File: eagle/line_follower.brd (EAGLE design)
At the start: 100 x 80 mm, 41 parts, among them IC1 A4950, IC2 A4950, IC3 MC78M05 (??), J1 2S - 4S LiPo, J2 22-27-2031-03, J3 22-27-2061-06, J4 22-27-2061-06, Q1 ALS-PT19-315C/L177/TR8, Q2 ALS-PT19-315C/L177/TR8, Q3 ALS-PT19-315C/L177/TR8, Q4 ALS-PT19-315C/L177/TR8, Q5 ALS-PT19-315C/L177/TR8, SW1 12MM_BUTTON, X1 ESP32DEVKITV1, X2 MPU6050_BREAKOUT

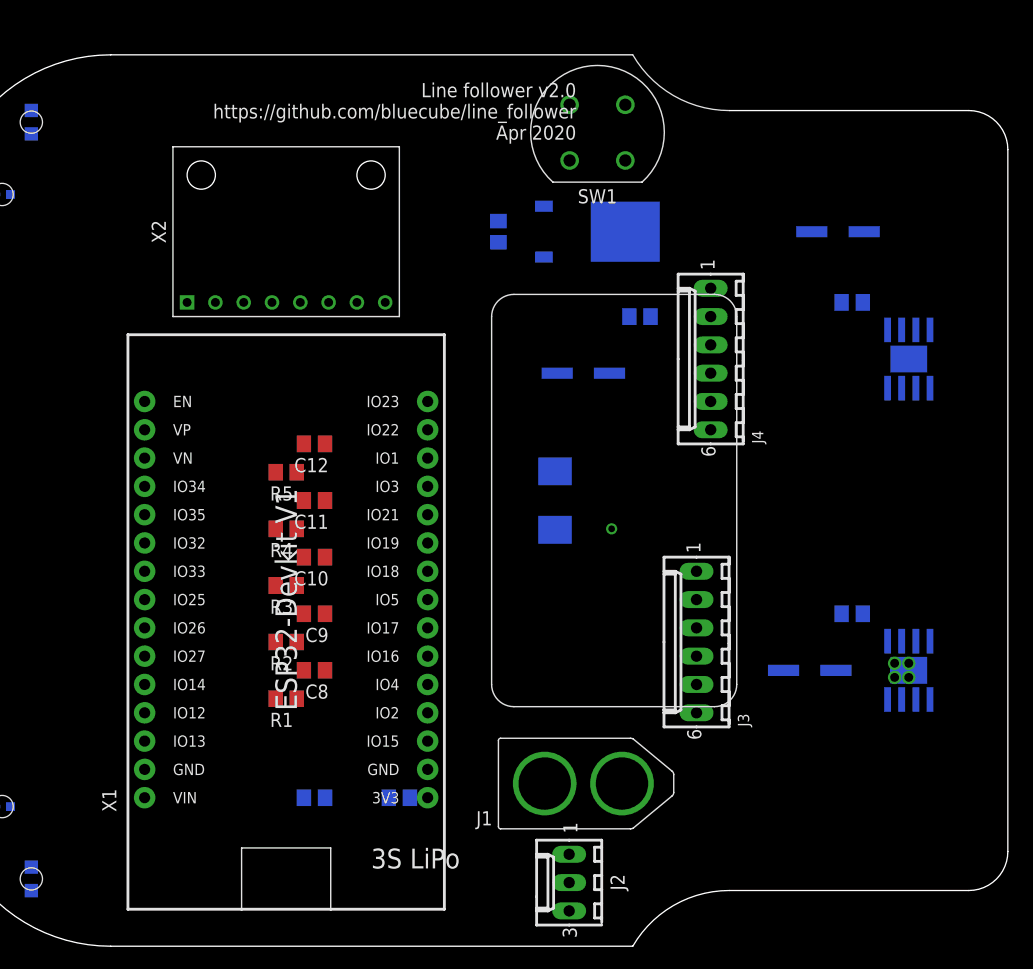
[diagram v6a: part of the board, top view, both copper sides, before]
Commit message: Decided to not use the encoder board on the motors, schematic tweaks and start of layout
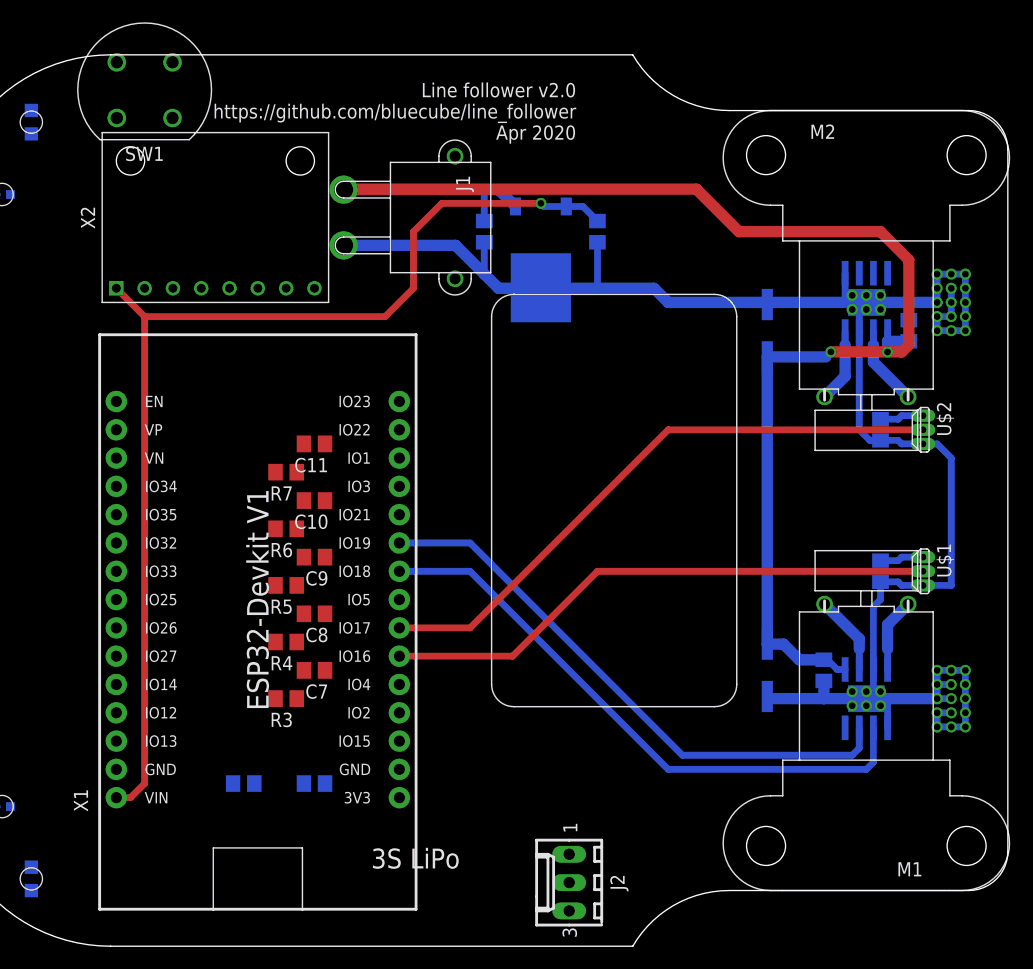
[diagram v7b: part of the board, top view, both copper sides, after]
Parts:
- removed D1: (no value), diode:MELF-MLL41
- removed J3, J4: 22-27-2061-06, con-molex:6410-06
- removed R10: 15k, rcl:R0805
- removed R9: 82k, rcl:R0805
- added C13: 100nF, rcl:C0805
- added M1, M2: N20-ENC, untitled:N20-ENC
- added R6, R7: 5k6, rcl:R0805
- added U$1, U$2: SI7202, untitled:TO92S
- C12: value 100n -> 100nF
- C2: value 100uF 25V -> 100nF; device rcl:UD-6,3X5,8_NICHICON -> rcl:C0805
- C6: value 100nF -> 22uF
- C7: value 100nF -> 100n
- IC3: value MC78M05 (??) -> NCV4274CDT50RKG
- J1: value 2S - 4S LiPo -> XT60PW-M; device RoboJackets-Connectors:XT-60_BARE -> untitled:XT60PW-M
- R1: value 5k6 -> 15k
- R2: value 5k6 -> 82k
- moved J1 51.6 mm to (45.7, 64.8)
- moved C12 50.8 mm to (88.9, 45.7), flipped to the bottom, turned to 270 degrees
- moved C5 47.6 mm to (53.3, 63.5), turned to 270 degrees
- moved C7 42.7 mm to (38.1, 24.1), flipped to the top, turned to 180 degrees
- moved SW1 40.8 mm to (22.9, 76.2)
- moved C1 31.4 mm to (78.7, 24.1), turned to 90 degrees
- moved C4 24.2 mm to (91.4, 54.6), turned to 90 degrees
- moved C6 23.7 mm to (63.5, 63.5), turned to 270 degrees
- moved R2 13.0 mm to (38.1, 14.0), flipped to the bottom, turned to 0 degrees
- moved C3 10.9 mm to (78.7, 54.6), turned to 270 degrees
- moved R3 10.2 mm to (35.6, 21.6)
- moved R4 10.2 mm to (35.6, 26.7)
- moved R5 10.2 mm to (35.6, 31.8)
- moved R1 8.52 mm to (31.8, 14.0), flipped to the bottom, turned to 0 degrees
- moved X2 6.48 mm to (29.2, 64.8)
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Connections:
- removed net ENCODER0A: J3.3
- removed net ENCODER0B: J3.4
- removed net ENCODER1A: J4.4, X1.28
- removed net ENCODER1B: J4.3, X1.6
- removed net N$6: C7.1, D1.A, IC3.2
- removed net N$7: C4.1, IC3.1
- removed net VCC: C2.+, C3.+, C5.1, C6.1, IC1.5, IC2.5, J1.+, R9.1
- new net ENCODER0: U$2.P$2, X1.7
- new net ENCODER1: U$1.P$2, X1.6
- new net VBAT: C1.+, C2.1, C3.+, C4.1, C5.1, IC1.5, IC2.5, IC3.1, J1.POS, R2.1
- net +3V3: now also C12.1, C13.1, U$1.P$1, U$2.P$1; no longer J3.2, J4.2
- net +5V: now also C6.1, IC3.2; no longer C1.+, D1.C
- net BAT_SENSE: now also R1.1, R2.2; no longer R10.1, R9.2
- net GND: now also C12.2, C13.2, C2.2, C7.1, J1.NEG, R1.2, R6.1, R7.1, U$1.P$3, U$2.P$3; no longer C12.1, C2.-, C7.2, J1.-, J3.5, J4.5, R1.1, R10.2, R2.1
- net LINE_SENSOR0: now also C7.2, R3.2; no longer C8.2, R1.2
- net LINE_SENSOR1: now also C8.2, R4.2; no longer C9.2, R2.2
- net LINE_SENSOR2: now also C9.2, R5.2; no longer C10.2, R3.2
- net LINE_SENSOR3: now also C10.2, R6.2; no longer C11.2, R4.2
- net LINE_SENSOR4: now also C11.2, R7.2; no longer C12.2, R5.2
- net MOTOR1A: now also X1.15
- net N$1: now also M1.P$2; no longer J3.1
- net N$2: now also M2.P$2; no longer J4.1
- net N$3: now also M2.P$1; no longer J4.6
- net N$4: now also M1.P$1; no longer J3.6
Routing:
- net GND: track 4.71 -> 181.5 mm, vias 4 -> 42
- net VBAT: track 0.00 -> 130.5 mm, vias 0 -> 2
- net +5V: track 0.00 -> 97.1 mm, vias 0 -> 1
- net ENCODER0: track 0.00 -> 54.4 mm
- net MOTOR0B: track 0.00 -> 53.3 mm
- net MOTOR0A: track 0.00 -> 51.3 mm
- net ENCODER1: track 0.00 -> 50.1 mm
- net +3V3: track 0.00 -> 7.89 mm
- net N$1: track 0.00 -> 7.15 mm
- net N$2: track 0.00 -> 7.15 mm
- net N$4: track 0.00 -> 6.63 mm
- net N$3: track 0.00 -> 6.63 mm

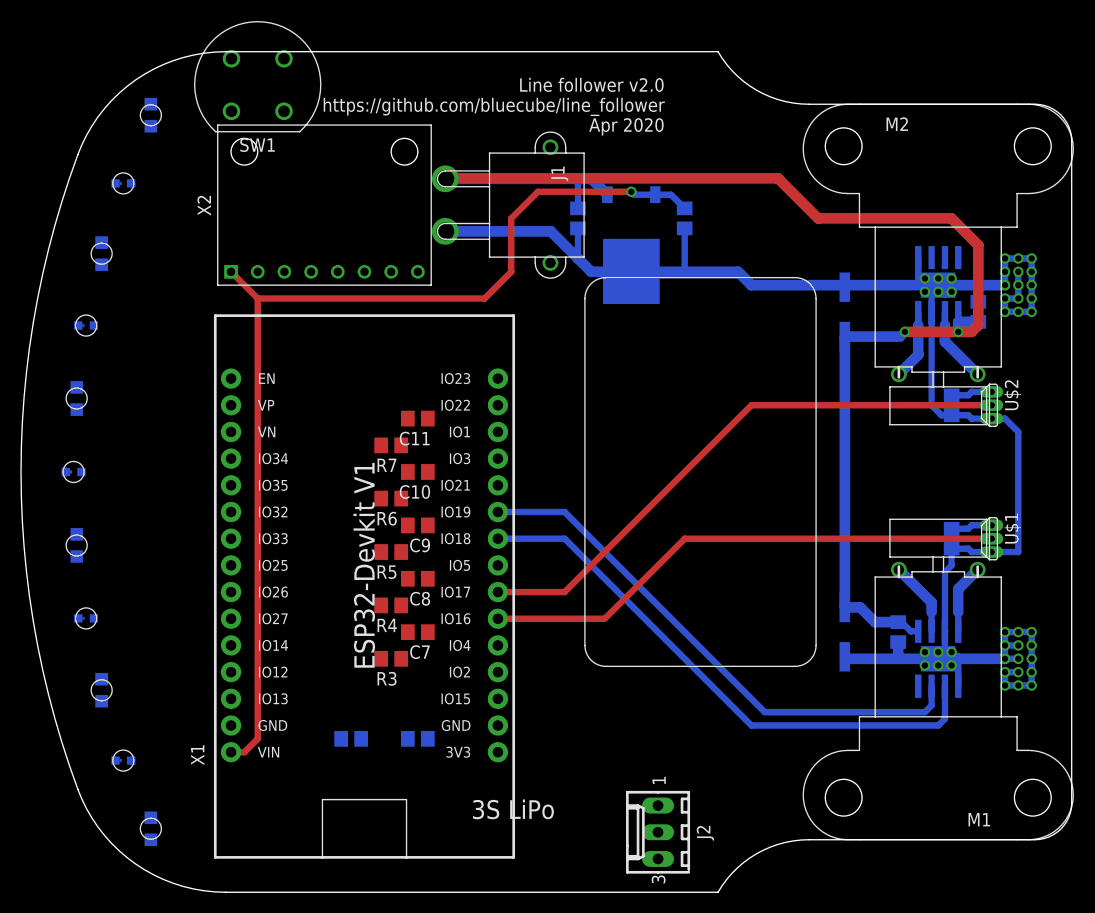
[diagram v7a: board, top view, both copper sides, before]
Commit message: Motor encoder boards are back, more layout work
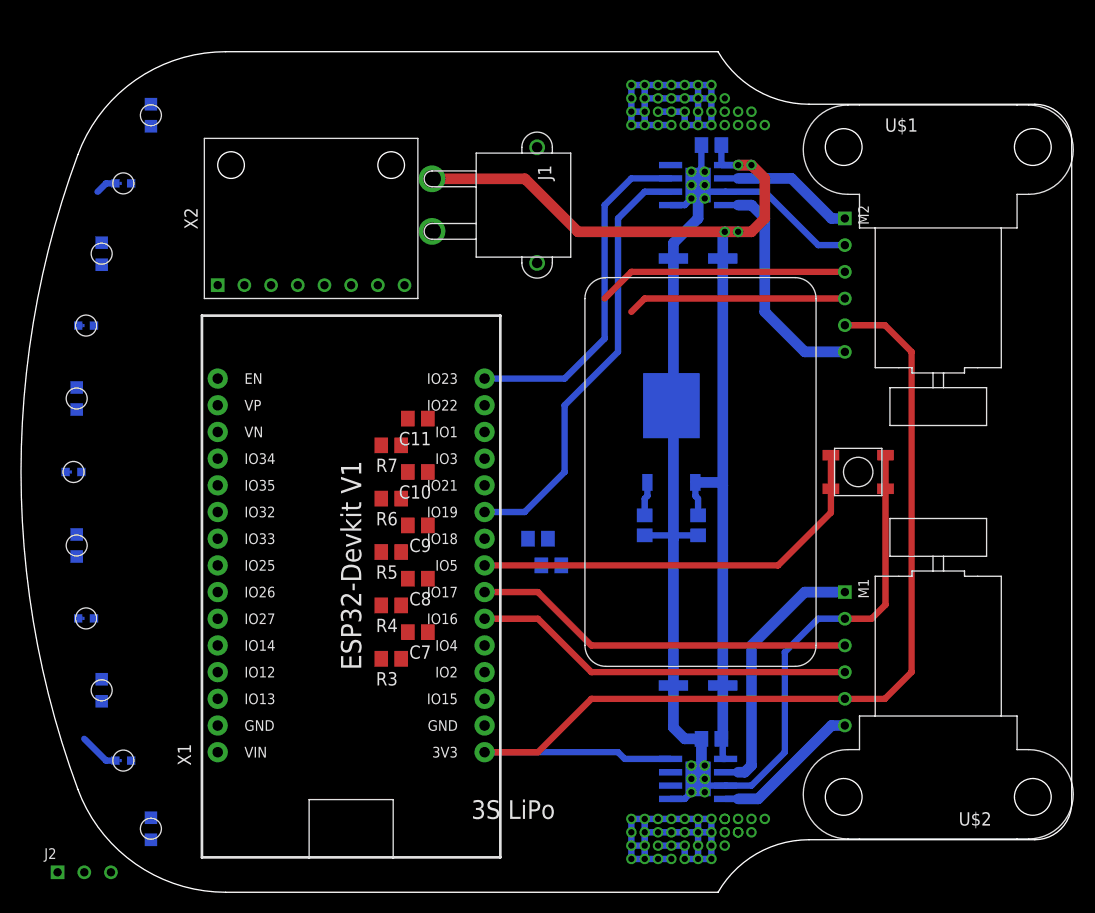
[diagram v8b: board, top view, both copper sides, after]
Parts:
- removed C12, C13: 100nF, rcl:C0805
- removed IC3: NCV4274CDT50RKG, linear:TO252
- removed SW1: 12MM_BUTTON, untitled:12MM_ROUND_BUTTON
- added IC5: NCV4274CDT50RKG, linear:TO252
- added S1: TACTILE-SWITCH, cube:SW4-SMD-4.5MM
- J2: value 22-27-2031-03 -> 2.54MM_HEADER_3X1; device con-molex:6410-03 -> untitled:2.54MM_HEADER_3X1
- M1, M2: value N20-ENC -> N20-ENC2; device untitled:N20-ENC -> untitled:2.54MM_HEADER_6X1
- U$1, U$2: value SI7202 -> (none); device untitled:TO92S -> untitled:N20-ENC-NOPIN
- moved J2 54.7 mm to (6.35, 1.27), turned to 0 degrees
- moved U$1 41.6 mm to (87.6, 74.3), turned to 0 degrees
- moved U$2 41.6 mm to (87.6, 4.45), turned to 180 degrees
- moved C5 31.4 mm to (64.8, 34.3)
- moved C4 30.0 mm to (66.0, 70.5), turned to 0 degrees
- moved C6 29.5 mm to (59.7, 34.3)
- moved R1 26.1 mm to (49.5, 33.0)
- moved IC1 25.6 mm to (64.8, 10.2), turned to 90 degrees
- moved IC2 24.8 mm to (64.8, 66.7), turned to 90 degrees
- moved R2 20.8 mm to (50.8, 30.5)
- moved C2 20.5 mm to (66.0, 14.0), turned to 0 degrees
- moved M2 19.4 mm to (78.7, 57.1), turned to 270 degrees
- moved M1 19.4 mm to (78.7, 21.6), turned to 270 degrees
- moved C1 14.9 mm to (64.8, 19.1), turned to 180 degrees
- moved C3 14.9 mm to (64.8, 59.7), turned to 180 degrees
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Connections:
- removed net ENCODER0: U$2.P$2, X1.7
- removed net ENCODER1: U$1.P$2, X1.6
- new net ACCEL_INT: X1.9, X2.P$8
- new net ENCODER0A: M1.P$3, X1.7
- new net ENCODER0B: M1.P$4, X1.6
- new net ENCODER1A: M2.P$4, X1.17
- new net ENCODER1B: M2.P$3, X1.18
- net +3V3: now also M1.P$5, M2.P$5; no longer C12.1, C13.1, U$1.P$1, U$2.P$1
- net +5V: now also IC5.2, J2.P$3; no longer IC3.2, J2.3
- net BAT_SENSE: now also X1.3; no longer X1.26
- net BUTTON: now also S1.P$1, S1.P$3; no longer SW1.A$1, SW1.A$2
- net GND: now also IC5.3, J2.P$2, M1.P$2, M2.P$2, S1.P$2, S1.P$4; no longer C12.2, C13.2, IC3.3, J2.2, SW1.B$1, SW1.B$2, U$1.P$3, U$2.P$3
- net LINE_SENSOR0: now also X1.22; no longer X1.21
- net LINE_SENSOR1: now also X1.26; no longer X1.3
- net LINE_SENSOR2: now also X1.21; no longer X1.22
- net MOTOR0A: now also X1.27; no longer X1.10
- net MOTOR0B: now also X1.28; no longer X1.9
- net MOTOR1A: now also X1.10; no longer X1.15
- net MOTOR1B: now also X1.15; no longer X1.27
- net N$1: now also M1.P$1; no longer M1.P$2
- net N$2: now also M2.P$1; no longer M2.P$2
- net N$3: now also M2.P$6; no longer M2.P$1
- net N$4: now also M1.P$6; no longer M1.P$1
- net RANGE: now also J2.P$1; no longer J2.1
- net VBAT: now also IC5.1; no longer IC3.1
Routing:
- net +3V3: track 7.89 -> 105.5 mm
- net +5V: track 97.1 -> 3.62 mm, vias 1 -> 0
- net ENCODER0: track 54.4 -> 0.00 mm
- net MOTOR0B: track 53.3 -> 0.00 mm
- net MOTOR0A: track 51.3 -> 0.00 mm
- net ENCODER1: track 50.1 -> 0.00 mm
- net MOTOR1A: track 0.00 -> 41.5 mm
- net BUTTON: track 0.00 -> 40.5 mm
- net ENCODER0B: track 0.00 -> 36.4 mm
- net ENCODER0A: track 0.00 -> 36.4 mm
- net MOTOR1B: track 0.00 -> 33.0 mm
- net GND: track 181.5 -> 154.0 mm, vias 42 -> 27
- net VBAT: track 130.5 -> 104.4 mm, vias 2 -> 4
- net ENCODER1B: track 0.00 -> 23.9 mm
- net ENCODER1A: track 0.00 -> 20.8 mm
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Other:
- board text added: "Line follower v2.0"
- board text added: "May 2020"
- board text added: "https://github.com/bluecube/line_follower"
- board text removed: "Line follower v2.0 https://github.com/bluecube/line_follower Apr 2020"
